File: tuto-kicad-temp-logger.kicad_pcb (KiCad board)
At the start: 4 copper layers, 62 parts, among them J201 HOOYA_USB_306F, J202 Conn_01x01_Pin, J401 SHOU HAN TF-CARD H1.8, Q301 L8050QLT1G, Q302 L8050QLT1G, SW301 TE_FSM4JSMATR, SW302 TE_FSM4JSMATR, U201 SGM2212-3.3XKC3G, U202 CP2102N-Axx-xQFN28, U301 ESP32-C3-WROOM-02, U401 TMP102xxDRL

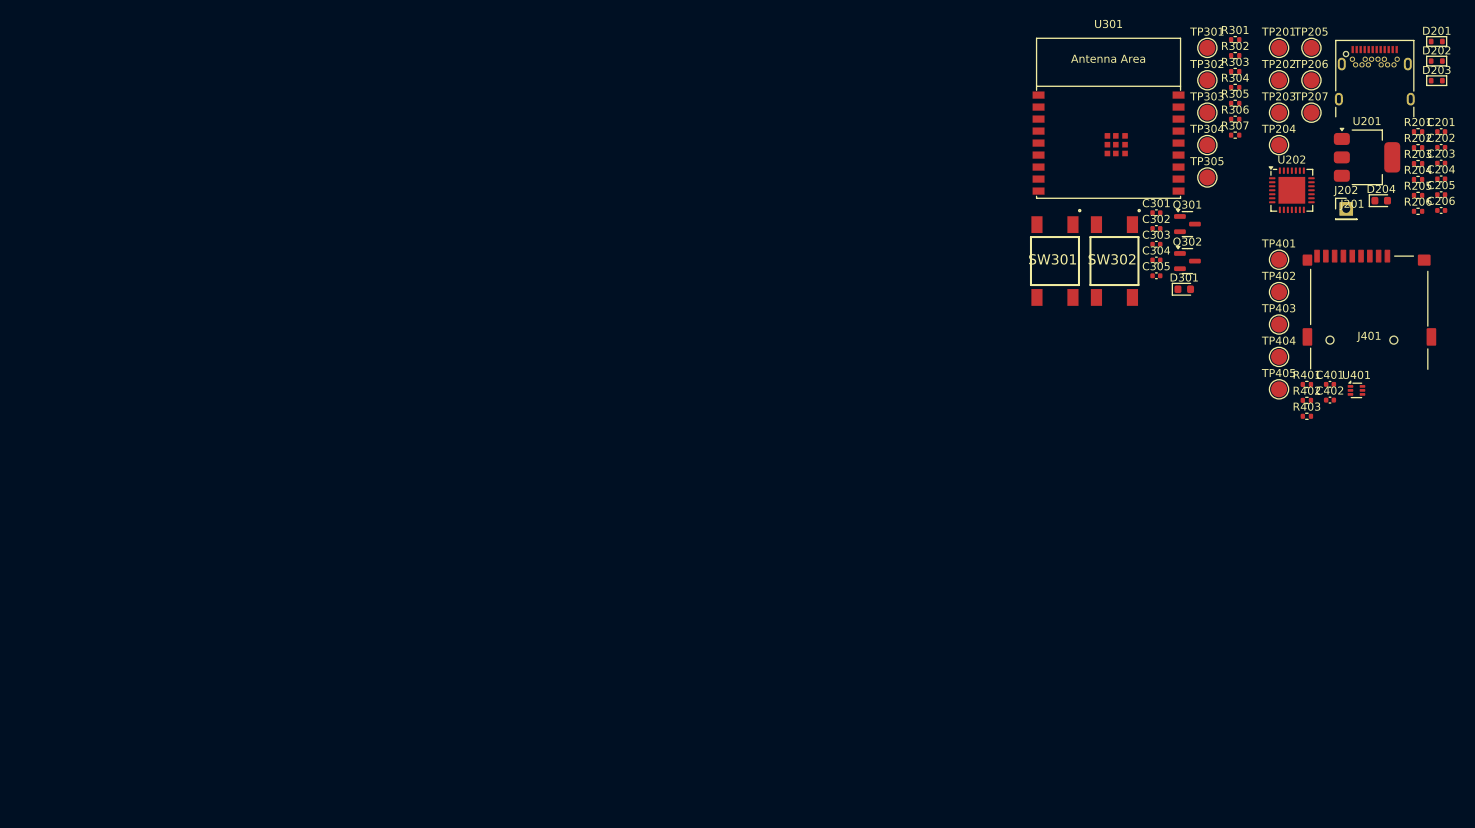
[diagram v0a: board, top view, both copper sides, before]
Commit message: Placement des composants
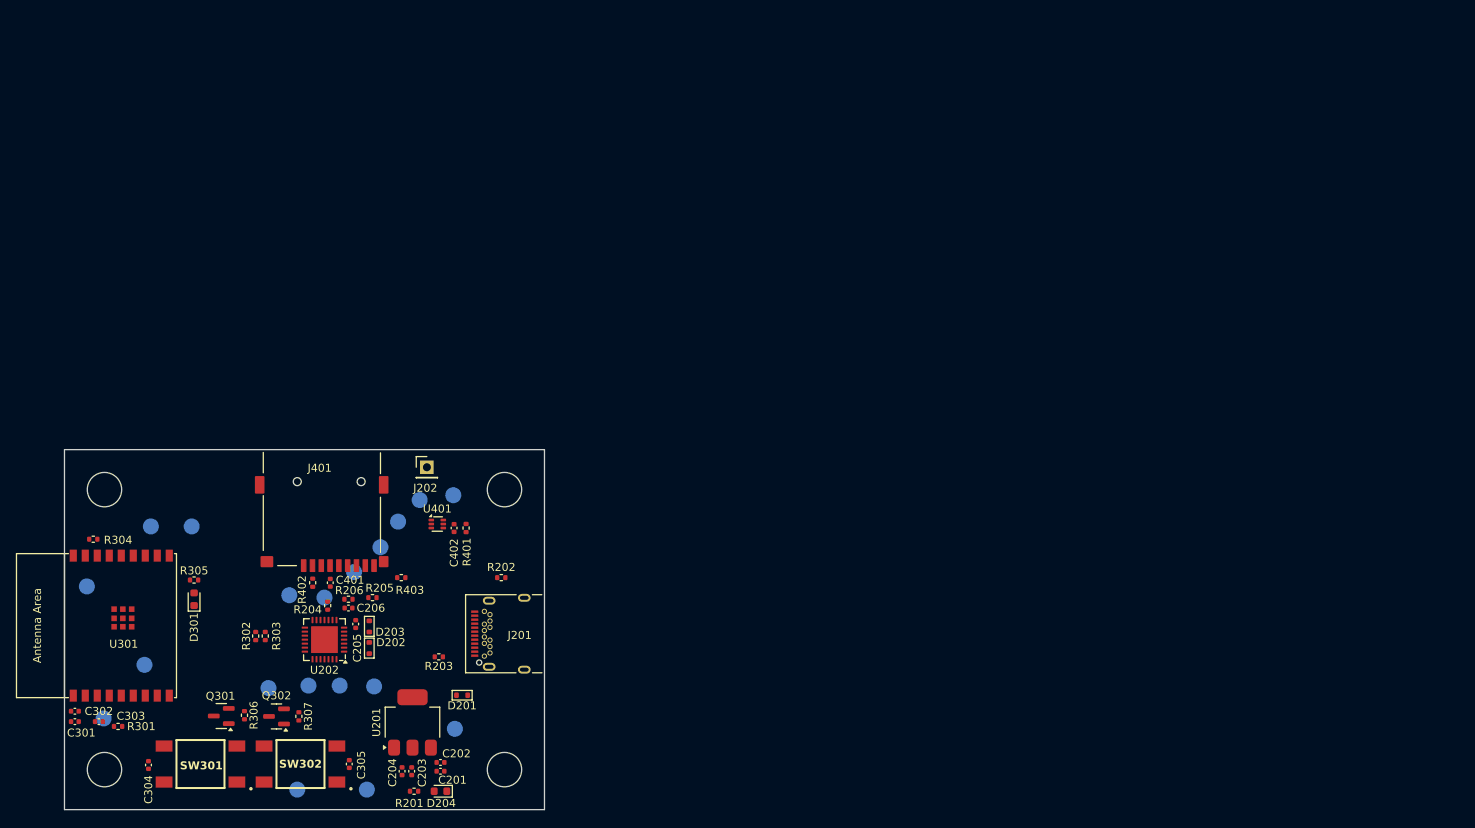
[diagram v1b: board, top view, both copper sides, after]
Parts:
- added H101: MountingHole, MountingHole:MountingHole_4.3mm_M4, F.Cu at (107.0, 81.0)
- added H102: MountingHole, MountingHole:MountingHole_4.3mm_M4, F.Cu at (157.0, 81.0)
- added H103: MountingHole, MountingHole:MountingHole_4.3mm_M4, F.Cu at (157.0, 116.0)
- added H104: MountingHole, MountingHole:MountingHole_4.3mm_M4, F.Cu at (107.0, 116.0)
- added TP406: TestPoint, TestPoint:TestPoint_Pad_D2.0mm, B.Cu at (150.6, 81.7)
- added TP407: TestPoint, TestPoint:TestPoint_Pad_D2.0mm, B.Cu at (146.4, 82.3)
- TP201, TP202, TP203, TP204, TP205, TP206, TP207, TP301, TP302, TP303, TP304, TP305, TP401, TP402, TP403, TP404, TP405: moved to B.Cu
- moved R301 163.9 mm to (108.7, 110.6), turned to 180 degrees
- moved TP301 161.4 mm to (106.9, 109.6), turned to 180 degrees
- moved R304 153.5 mm to (105.6, 87.2)
- moved TP205 153.0 mm to (127.5, 105.8), turned to 180 degrees
- moved TP207 152.4 mm to (131.1, 118.5), turned to 180 degrees
- moved D202 152.3 mm to (140.1, 100.8), turned to 90 degrees
- moved TP303 152.1 mm to (104.8, 93.1), turned to 180 degrees
- moved R201 150.2 mm to (145.7, 118.7)
- moved D203 149.9 mm to (140.1, 98.1), turned to -90 degrees
- moved C204 149.5 mm to (144.2, 116.2), turned to -90 degrees
- moved C203 149.5 mm to (145.4, 116.2), turned to -90 degrees
- moved C301 149.4 mm to (103.3, 110.0)
- moved C201 148.5 mm to (149.0, 116.2)
- moved C302 148.0 mm to (103.3, 108.7)
- moved TP304 147.9 mm to (112.0, 102.9), turned to 180 degrees
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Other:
- board outline added: 60 x 45 mm
